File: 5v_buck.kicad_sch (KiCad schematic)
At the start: 16 parts, among them U3 TPS54540BDDA

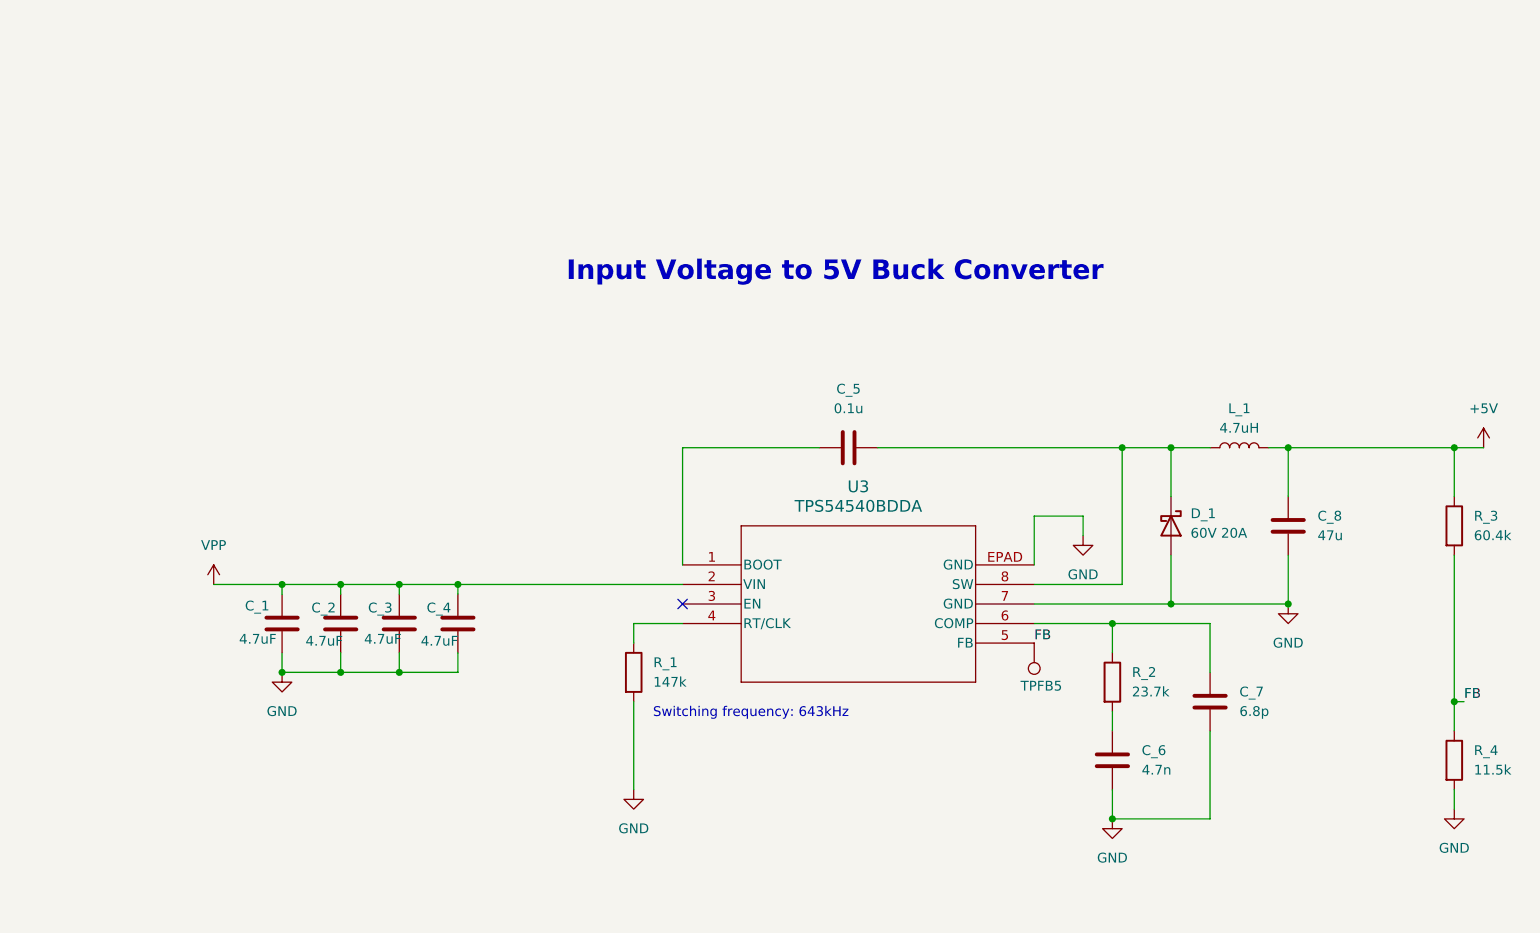
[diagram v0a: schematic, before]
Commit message: Rename references, update symbols and schematic layout
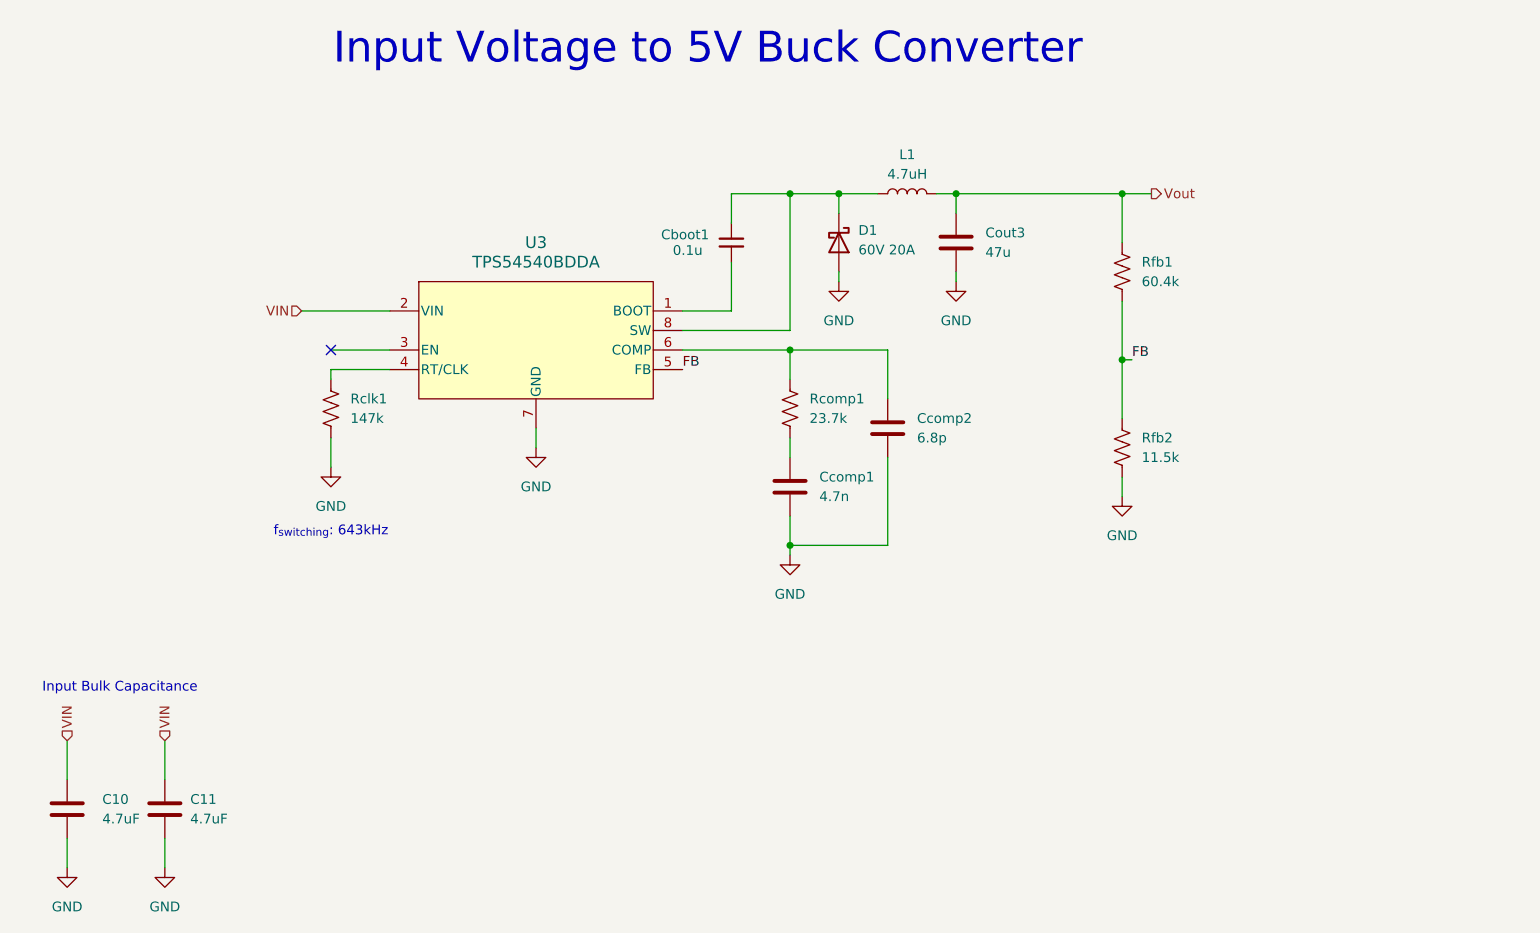
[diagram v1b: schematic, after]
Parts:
- removed C_1, C_2, C_3, C_4: 4.7uF, Capacitor_SMD:C_0805_2012Metric, symbol Device:C
- removed C_5: 0.1u, Capacitor_SMD:C_0805_2012Metric, symbol Device:C
- removed TPFB5: TestPoint, TestPoint:TestPoint_Loop_D2.60mm_Drill0.9mm_Beaded, symbol Connector:TestPoint
- added C10, C11: 4.7uF, Capacitor_SMD:C_0805_2012Metric, symbol Device:C
- added Cboot1: 0.1u, Capacitor_SMD:C_0805_2012Metric, symbol Device:C_Small
- Rclk1: renamed from R_1; symbol Device:R -> Device:R_US
- Rcomp1: renamed from R_2; symbol Device:R -> Device:R_US
- Rfb1: renamed from R_3; symbol Device:R -> Device:R_US
- Rfb2: renamed from R_4; symbol Device:R -> Device:R_US
- U3: symbol 2026-07-22_15-59-22:TPS54540BDDA -> LEOS:TPS54540BDDA
- renumbered C_6 to Ccomp1, C_7 to Ccomp2, C_8 to Cout3, D_1 to D1, L_1 to L1
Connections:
- net GND: now also C10.2, C11.2
- net at U3.1 (BOOT): now also Cboot1.1
- net at D1.1 (K), L1.1, U3.8 (SW): now also Cboot1.2
- net +5V renamed Vout
- net VPP renamed VIN
- net VIN: now also C10.1, C11.1
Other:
- note added: "Input Bulk Capacitance"
- note added: "f_{switching}: 643kHz"
- note removed: "Switching frequency: 643kHz"
- company: (none) -> VIP Lightning From the Edge of Space
- moved on the sheet: Ccomp1, Ccomp2, Cout3, D1, L1
